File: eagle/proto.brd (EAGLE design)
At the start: 68 x 70.5 mm, 15 parts, among them J1 DCJ0202, X1 NRF51822-RIGHT

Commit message: eagle: Kolejna wersja prototypu
Signed-off-by: Pawel Szewczyk <pfpawelec@gmail.com>
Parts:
- added DEC+, DEC-, RA+, RA-: TACT-SWITCH, eq-custom2:TACT-SWITCH-THT
- added LED3, LED4: (no value), led:LED3MM
- added R3, R4: (no value), eagle-ltspice:0204/7
- moved LED1 4.03 mm to (21.0, 56.5)
- moved LED2 4.03 mm to (26.0, 56.5)
- moved R1 4.03 mm to (21.0, 48.5)
- moved R2 4.03 mm to (26.0, 48.5)
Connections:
- new net DEC+: DEC+.P$1, X1.8
- new net DEC-: DEC-.P$1, X1.10
- new net LED3: R3.2, U$1.5
- new net LED4: R4.2, U$1.3
- new net N$3: LED3.A, R3.1
- new net N$6: LED4.A, R4.1
- new net RA+: RA+.P$1, X1.7
- new net RA-: RA-.P$1, X1.9
- net +3V3: now also UART0.2
- net GND: now also DEC+.P$2, DEC-.P$2, LED3.K, LED4.K, RA+.P$2, RA-.P$2, U$1.12
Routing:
- net GND: track 223.7 -> 93.0 mm, vias 0 -> 10
- net RA+: track 0.00 -> 40.3 mm, vias 0 -> 2
- net RA-: track 0.00 -> 35.3 mm, vias 0 -> 2
- net +3V3: track 132.7 -> 164.1 mm
- net SWD: track 53.0 -> 28.2 mm
- net DEC+: track 0.00 -> 19.3 mm
- net LED3: track 0.00 -> 10.9 mm
- net DEC-: track 0.00 -> 10.1 mm
- net LED4: track 0.00 -> 5.07 mm
- net N$6: track 0.00 -> 2.92 mm
- net N$3: track 0.00 -> 2.92 mm
- net LED2: track 14.6 -> 16.7 mm
- net LED1: track 20.4 -> 22.6 mm
- net DEC-STEP: track 12.6 -> 11.7 mm
- net TX: track 23.4 -> 22.5 mm, vias 0 -> 2
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- added copper zone on layer 1, net GND

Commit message: board: Change some elements to 	smd
Signed-off-by: Pawel Szewczyk <pfpawelec@gmail.com>
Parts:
- C2: device rcl:E2,5-6 -> rcl:SMC_C
- LED1, LED2, LED3, LED4: device led:LED3MM -> led:SML1206
- R1, R2, R3, R4: device eagle-ltspice:0204/7 -> eagle-ltspice:R1206
- turned LED1 to 270 degrees
- turned LED2 to 270 degrees
- turned LED3 to 270 degrees
- turned LED4 to 270 degrees
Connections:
- net GND: now also LED1.C, LED2.C, LED3.C, LED4.C; no longer LED1.K, LED2.K, LED3.K, LED4.K
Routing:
- net GND: track 93.0 -> 87.6 mm, vias 10 -> 8
- net LED1: track 22.6 -> 25.1 mm, vias 0 -> 1
- net LED2: track 16.7 -> 18.7 mm, vias 0 -> 1
- net LED4: track 5.07 -> 7.02 mm, vias 0 -> 1
- net N$6: track 2.92 -> 4.83 mm
- net N$3: track 2.92 -> 4.83 mm
- net N$2: track 2.92 -> 4.83 mm
- net N$1: track 2.92 -> 4.83 mm
- net LED3: track 10.9 -> 12.6 mm, vias 0 -> 1
- net +12V: track 55.2 -> 53.9 mm
- net SWD: track 28.2 -> 28.7 mm, vias 0 -> 2
- net RTS: track 25.9 -> 25.8 mm, vias 2 -> 0
- net TX: vias 2 -> 0
- net RX: track 25.5 -> 25.4 mm, vias 2 -> 0
- net CTS: vias 2 -> 0

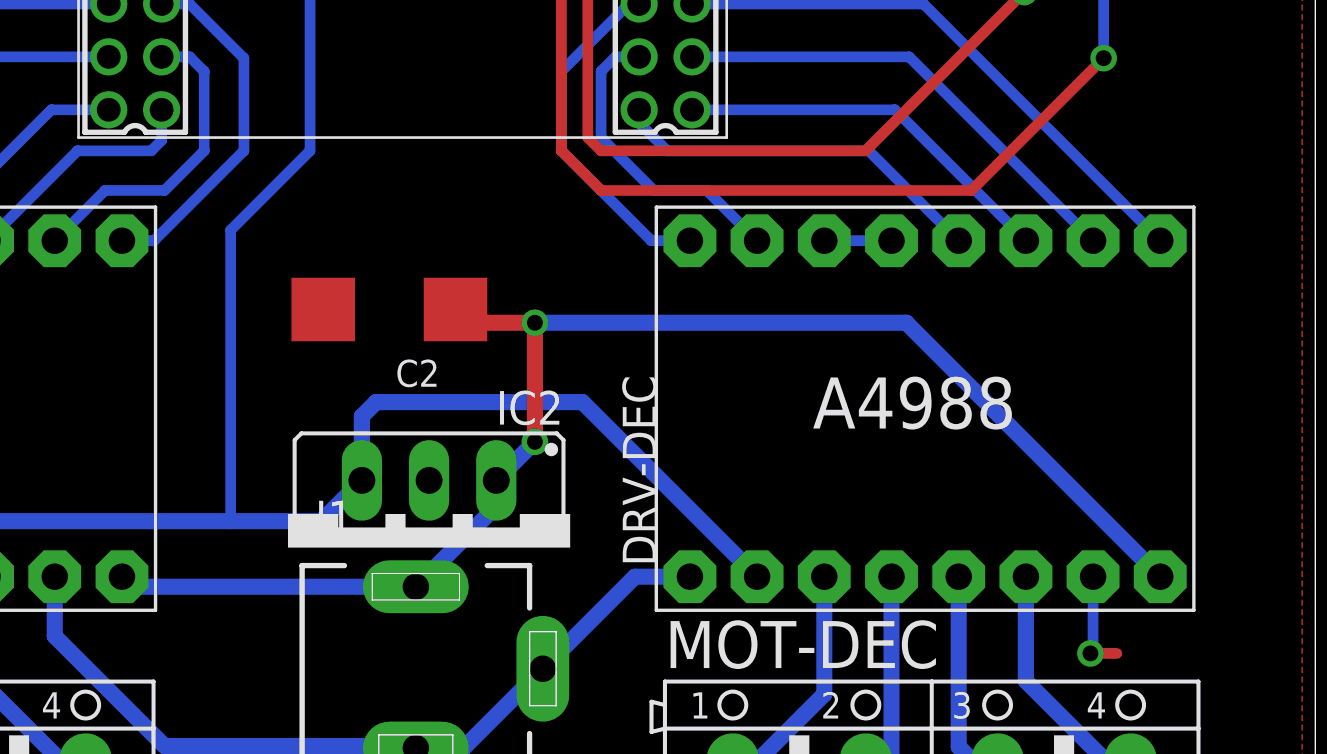
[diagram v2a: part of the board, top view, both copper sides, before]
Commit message: Change more elements to smd
Signed-off-by: Pawel Szewczyk <pfpawelec@gmail.com>
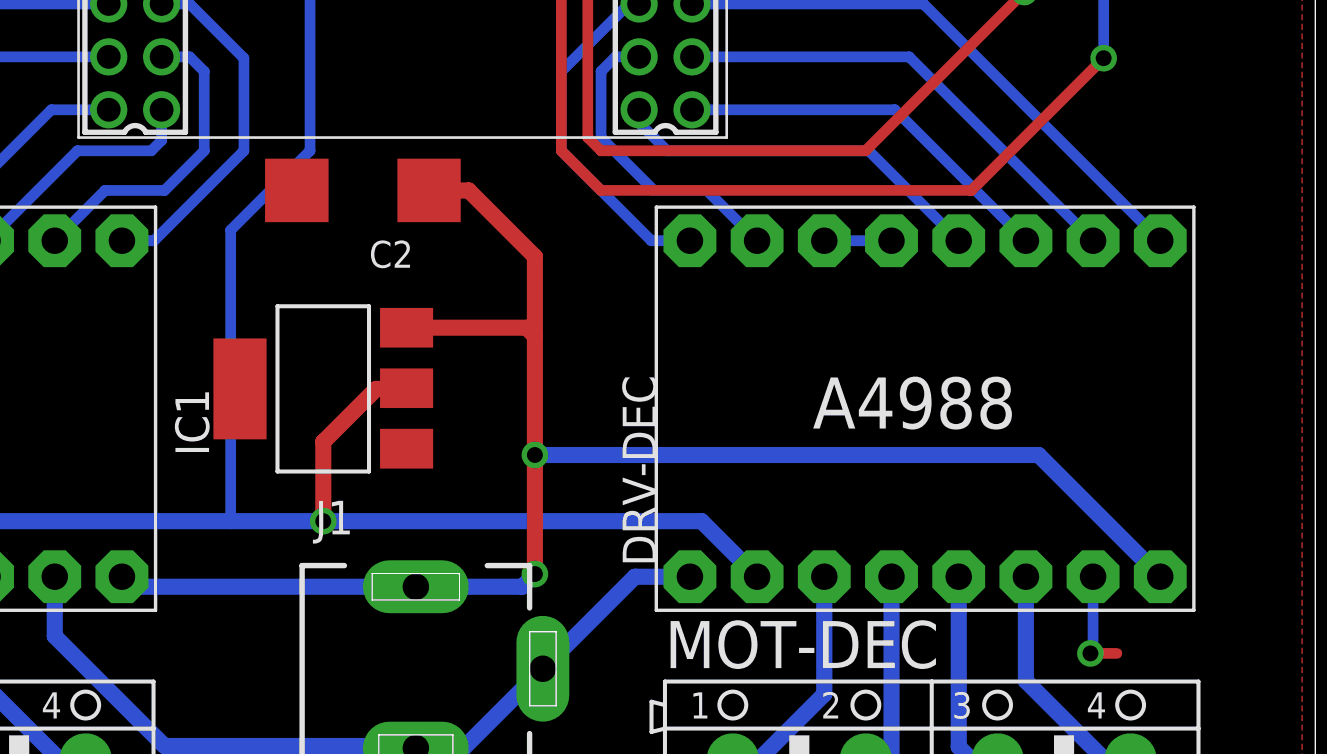
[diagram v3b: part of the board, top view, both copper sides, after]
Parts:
- removed IC2: (no value), lf33:TO220S
- added IC1: REG1117, burr-brown:SOT223
- moved C2 4.61 mm to (50.0, 26.0)
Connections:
- net +12V: now also IC1.3; no longer IC2.1
- net +3V3: now also IC1.2; no longer IC2.3
- net GND: now also IC1.1; no longer IC2.2
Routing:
- net +12V: track 53.9 -> 63.8 mm
- net +3V3: track 164.1 -> 165.9 mm, vias 0 -> 1
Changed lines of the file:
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@@
 <attribute name="OC_NEWARK" value="unknown" x="71.5" y="3.5" size="1.778" layer="27" display="off"/>
 </element>
-<element name="IC2" library="lf33" package="TO220S" value="" x="52.5" y="12.5" rot="R180"/>
-<element name="C2" library="rcl" package="SMC_C" value="" x="51" y="21.5" rot="R180"/>
+<element name="C2" library="rcl" package="SMC_C" value="" x="50" y="26" rot="R180"/>
 <element name="LED1" library="led" package="SML1206" value="" x="21" y="56.5" rot="R270"/>
 <element name="LED2" library="led" package="SML1206" value="" x="26" y="56.5" rot="R270"/>
@@
 <attribute name="SPICEPREFIX" value="R" x="36" y="48.5" size="1.778" layer="27" rot="R270" display="off"/>
 </element>
+<element name="IC1" library="burr-brown" package="SOT223" value="REG1117" x="48.5" y="18.5" rot="R90">
+<attribute name="MF" value="" x="48.5" y="18.5" size="1.778" layer="27" rot="R90" display="off"/>
+<attribute name="MPN" value="REG1117" x="48.5" y="18.5" size="1.778" layer="27" rot="R90" display="off"/>
+<attribute name="OC_FARNELL" value="1097566" x="48.5" y="18.5" size="1.778" layer="27" rot="R90" display="off"/>
+<attribute name="OC_NEWARK" value="14P6981" x="48.5" y="18.5" size="1.778" layer="27" rot="R90" display="off"/>
+</element>
 </elements>
 <signals>
@@
 <contactref element="DRV-DEC" pad="P16"/>
 <contactref element="DRV-DEC" pad="P10"/>
-<contactref element="IC2" pad="2"/>
 <contactref element="C2" pad="-"/>
 <contactref element="LED1" pad="C"/>
@@
 <wire x1="82" y1="40.5" x2="78" y2="40.5" width="0.4064" layer="16"/>
 <wire x1="78" y1="40.5" x2="78" y2="40.65" width="0.4064" layer="16"/>
+<contactref element="IC1" pad="1"/>
+<wire x1="82" y1="40.5" x2="82.5" y2="48" width="0" layer="19" extent="1-1"/>
+<wire x1="62" y1="61" x2="69.5" y2="49.15" width="0" layer="19" extent="1-1"/>
+<wire x1="36" y1="58.25" x2="53.5" y2="61" width="0" layer="19" extent="1-16"/>
+<wire x1="31" y1="58.25" x2="36" y2="58.25" width="0" layer="19" extent="1-1"/>
+<wire x1="26" y1="58.25" x2="31" y2="58.25" width="0" layer="19" extent="1-1"/>
+<wire x1="21" y1="58.25" x2="26" y2="58.25" width="0" layer="19" extent="1-1"/>
+<wire x1="40.5" y1="47.5" x2="36" y2="58.25" width="0" layer="19" extent="1-1"/>
+<wire x1="42.39" y1="35.05" x2="40.39" y2="45.05" width="0" layer="19" extent="1-1"/>
+<wire x1="47.5" y1="26" x2="42.39" y2="35.05" width="0" layer="19" extent="1-1"/>
+<wire x1="38.35" y1="11.4" x2="47.5" y2="26" width="0" layer="19" extent="1-1"/>
+<wire x1="77.6" y1="11.4" x2="62.36" y2="11.4" width="0" layer="19" extent="1-1"/>
+<wire x1="23.11" y1="11.4" x2="38.35" y2="11.4" width="0" layer="19" extent="1-1"/>
+<wire x1="51.6496" y1="16.2394" x2="23.11" y2="11.4" width="0" layer="19" extent="1-1"/>
 </signal>
 <signal name="+12V">
@@
 <contactref element="DRV-RA" pad="P9"/>
 <contactref element="DRV-DEC" pad="P9"/>
-<contactref element="IC2" pad="1"/>
 <contactref element="C2" pad="+"/>
 <wire x1="40.89" y1="11.4" x2="41.27" y2="11.02" width="0.6096" layer="16"/>
 <wire x1="41.27" y1="11.02" x2="52" y2="11.02" width="0.6096" layer="16"/>
-<wire x1="52" y1="11.02" x2="55.04" y2="14.06" width="0.6096" layer="16"/>
-<wire x1="55.04" y1="14.06" x2="55.04" y2="15.04" width="0.6096" layer="16"/>
-<wire x1="55.04" y1="15.04" x2="56.5" y2="16.5" width="0.6096" layer="16"/>
-<via x="56.5" y="16.5" extent="1-16" drill="0.6" shape="square"/>
-<via x="56.5" y="21" extent="1-16" drill="0.6" shape="square"/>
-<wire x1="56.5" y1="16.5" x2="56.5" y2="21" width="0.6096" layer="1"/>
-<wire x1="56.5" y1="21" x2="70.54" y2="21" width="0.6096" layer="16"/>
-<wire x1="70.54" y1="21" x2="80.14" y2="11.4" width="0.6096" layer="16"/>
-<wire x1="56.5" y1="21" x2="54" y2="21" width="0.6096" layer="1"/>
-<wire x1="54" y1="21" x2="53.5" y2="21.5" width="0.6096" layer="1"/>
+<via x="56.5" y="11.5" extent="1-16" drill="0.6" shape="square"/>
+<via x="56.5" y="16" extent="1-16" drill="0.6" shape="square"/>
+<contactref element="IC1" pad="3"/>
+<wire x1="51.8382" y1="21" x2="51.6496" y2="20.8114" width="0.6096" layer="1"/>
+<wire x1="52" y1="11.02" x2="56.02" y2="11.02" width="0.6096" layer="16"/>
+<wire x1="56.02" y1="11.02" x2="56.5" y2="11.5" width="0.6096" layer="16"/>
+<wire x1="56.5" y1="16" x2="75.54" y2="16" width="0.6096" layer="16"/>
+<wire x1="75.54" y1="16" x2="80.14" y2="11.4" width="0.6096" layer="16"/>
+<wire x1="56.5" y1="11.5" x2="56.5" y2="16" width="0.6096" layer="1"/>
+<wire x1="56.5" y1="20.5" x2="56.5" y2="16" width="0.6096" layer="1"/>
+<wire x1="56.5" y1="20.5" x2="56.5" y2="23.5" width="0.6096" layer="1"/>
+<wire x1="56.5" y1="23.5" x2="54" y2="26" width="0.6096" layer="1"/>
+<wire x1="54" y1="26" x2="52.5" y2="26" width="0.6096" layer="1"/>
+<wire x1="51.6496" y1="20.8114" x2="56.1886" y2="20.8114" width="0.6096" layer="1"/>
+<wire x1="56.1886" y1="20.8114" x2="56.5" y2="20.5" width="0.6096" layer="1"/>
 </signal>
 <signal name="+3V3">
@@
 <contactref element="DRV-RA" pad="P15"/>
 <contactref element="DRV-DEC" pad="P15"/>
-<contactref element="IC2" pad="3"/>
 <contactref element="UART0" pad="2"/>
 <wire x1="25.65" y1="12.65" x2="25.65" y2="11.4" width="0.6096" layer="16"/>
 <wire x1="25.65" y1="12.65" x2="26.5" y2="13.5" width="0.6096" layer="16"/>
 <wire x1="26.5" y1="13.5" x2="45" y2="13.5" width="0.6096" layer="16"/>
-<wire x1="45" y1="13.5" x2="48.42" y2="13.5" width="0.6096" layer="16"/>
-<wire x1="48.42" y1="13.5" x2="49.96" y2="15.04" width="0.6096" layer="16"/>
-<wire x1="49.96" y1="15.04" x2="49.96" y2="17.46" width="0.6096" layer="16"/>
-<wire x1="49.96" y1="17.46" x2="50.5" y2="18" width="0.6096" layer="16"/>
-<wire x1="50.5" y1="18" x2="58.3" y2="18" width="0.6096" layer="16"/>
-<wire x1="58.3" y1="18" x2="64.9" y2="11.4" width="0.6096" layer="16"/>
 <wire x1="25.65" y1="11.4" x2="23.75" y2="9.5" width="0.4064" layer="16"/>
 <wire x1="23.75" y1="9.5" x2="21.5" y2="9.5" width="0.4064" layer="16"/>
@@
 <wire x1="64.44" y1="64.56" x2="64.44" y2="63.75" width="0.4064" layer="16"/>
 <wire x1="49" y1="66" x2="63" y2="66" width="0.4064" layer="16"/>
+<contactref element="IC1" pad="2"/>
+<wire x1="45" y1="13.5" x2="48.5" y2="13.5" width="0.6096" layer="16"/>
+<via x="48.5" y="13.5" extent="1-16" drill="0.6" shape="square"/>
+<wire x1="48.5" y1="13.5" x2="48.5" y2="16.5" width="0.6096" layer="1"/>
+<wire x1="48.5" y1="16.5" x2="50.5" y2="18.5" width="0.6096" layer="1"/>
+<wire x1="50.5" y1="18.5" x2="51.6242" y2="18.5" width="0.6096" layer="1"/>
+<wire x1="51.6242" y1="18.5" x2="51.6496" y2="18.5254" width="0.6096" layer="1"/>
+<wire x1="48.5" y1="13.5" x2="62.8" y2="13.5" width="0.6096" layer="16"/>
+<wire x1="62.8" y1="13.5" x2="64.9" y2="11.4" width="0.6096" layer="16"/>
 </signal>
 <signal name="TX">

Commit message: eagle: Add ST4 port
Signed-off-by: Pawel Szewczyk <pfpawelec@gmail.com>
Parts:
- removed LED4: (no value), led:SML1206
- removed R4: (no value), eagle-ltspice:R1206
- added ST4: RJ11, SparkFun-Connectors:RJ11-6
- moved RA+ 54.5 mm to (23.5, 39.0), turned to 180 degrees
- moved RA- 46.5 mm to (23.5, 31.0), turned to 180 degrees
- moved DEC- 19.4 mm to (80.5, 30.5), turned to 0 degrees
- moved DEC+ 7.91 mm to (80.5, 39.0), turned to 0 degrees
- moved LED1 6.73 mm to (26.0, 61.0)
- moved LED2 6.73 mm to (31.0, 61.0)
- moved LED3 6.73 mm to (36.0, 61.0)
- moved R1 6.73 mm to (26.0, 53.0)
- moved R2 6.73 mm to (31.0, 53.0)
- moved R3 6.73 mm to (36.0, 53.0)
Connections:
- removed net LED4: R4.2, U$1.3
- removed net N$6: LED4.A, R4.1
- net DEC+: now also ST4.4
- net DEC-: now also ST4.5
- net GND: now also ST4.2; no longer LED4.C
- net LED2: now also U$1.5; no longer U$1.7
- net LED3: now also U$1.3; no longer U$1.5
- net RA+: now also ST4.3
- net RA-: now also ST4.6
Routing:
- net DEC-: track 10.1 -> 61.8 mm
- net RA-: track 35.3 -> 83.3 mm
- net RA+: track 40.3 -> 65.4 mm
- net DEC+: track 19.3 -> 28.9 mm
- net GND: track 87.6 -> 80.6 mm, vias 8 -> 9
- net LED4: track 7.02 -> 0.00 mm, vias 1 -> 0
- net N$6: track 4.83 -> 0.00 mm
- net +3V3: track 165.9 -> 161.7 mm
- net LED1: track 25.1 -> 21.7 mm
- net LED2: track 18.7 -> 15.6 mm
- net RTS: track 25.8 -> 27.3 mm
- net LED3: track 12.6 -> 11.6 mm
